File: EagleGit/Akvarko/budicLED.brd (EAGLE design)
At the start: 118.1 x 101.6 mm, 50 parts, among them IC1 7805TV, Q1 BD243C, Q2 BD243C, Q3 BD243C, Q4 BD243C, T1 2N5551, T2 2N5551, T3 2N5551, T4 2N5551, X1 SMKDSP_1,5/2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

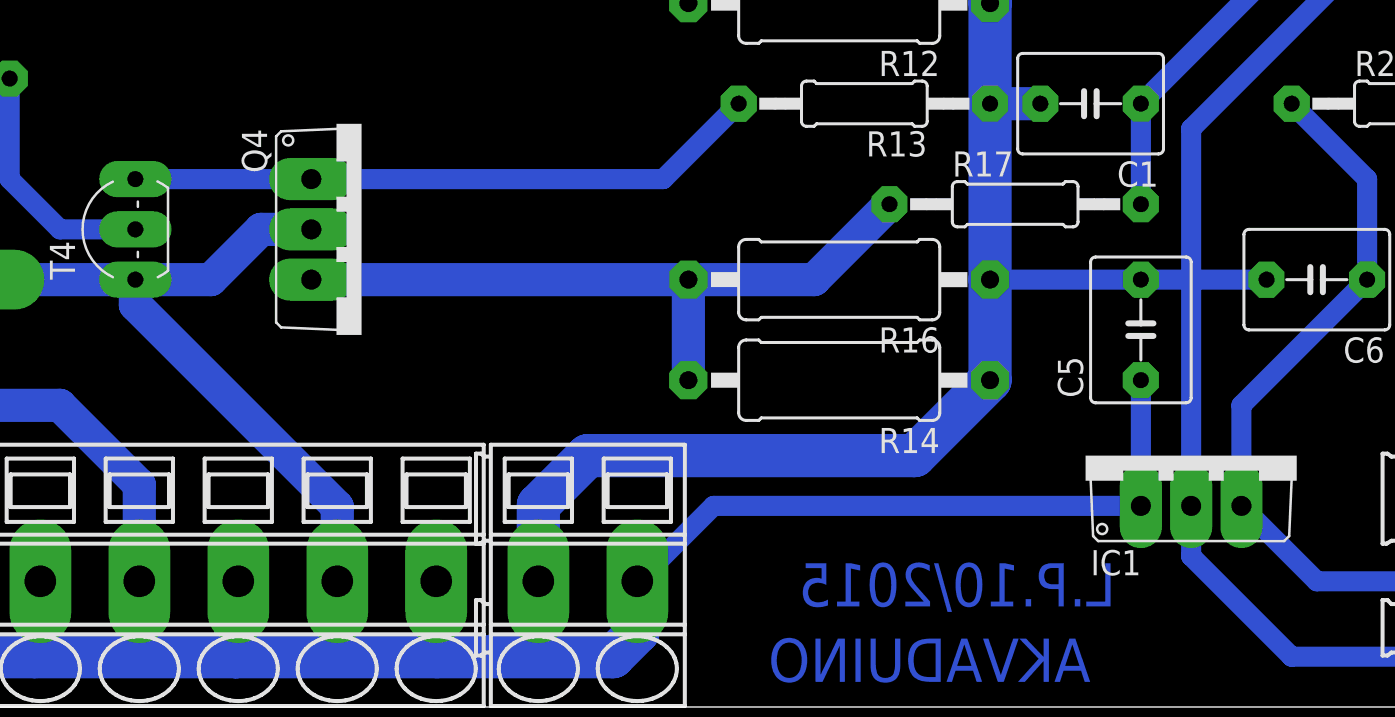
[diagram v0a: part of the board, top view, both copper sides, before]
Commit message: Vytvorena cela pro Rogowskiho civku a dodelan budic LED
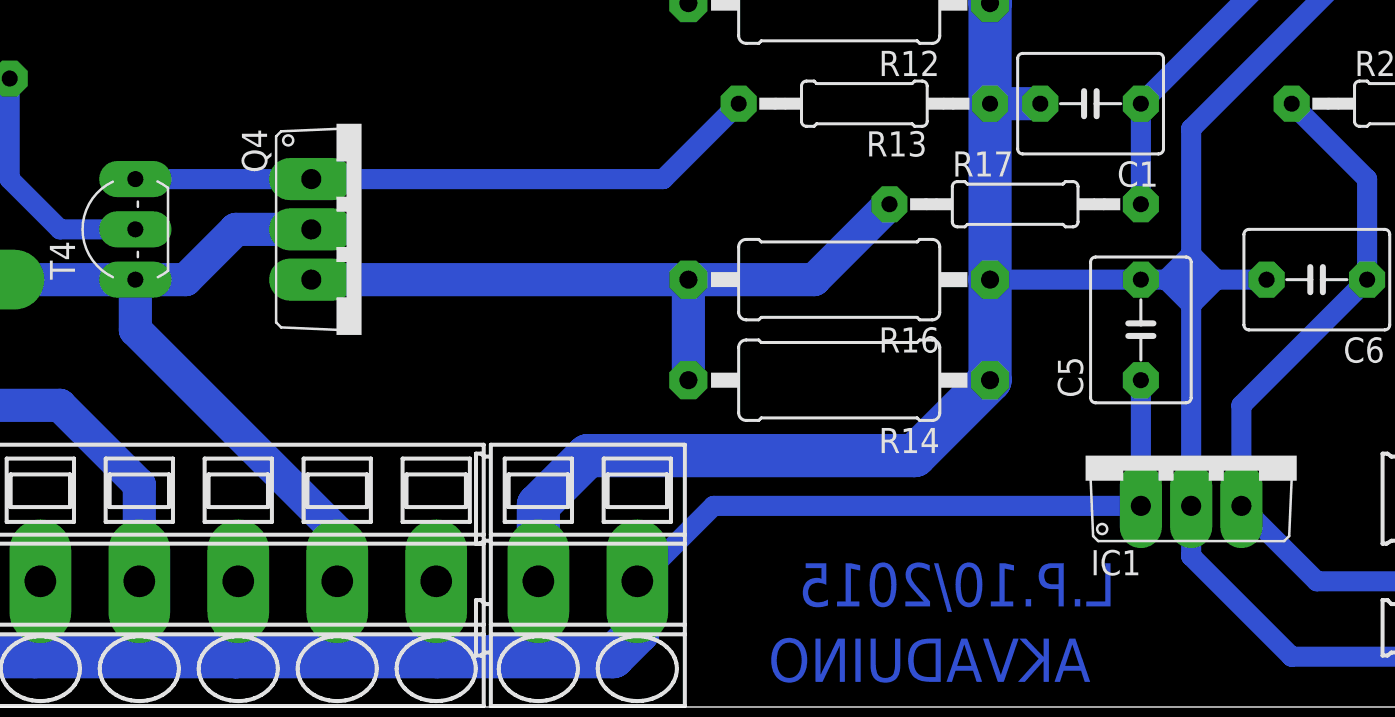
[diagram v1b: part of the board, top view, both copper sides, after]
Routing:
- net GND: track 554.0 -> 561.2 mm
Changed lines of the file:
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@@
 <contactref element="C6" pad="2"/>
 <contactref element="C7" pad="-"/>
-<wire x1="85.09" y1="21.59" x2="85.09" y2="10.16" width="1.016" layer="16"/>
+<wire x1="85.09" y1="21.59" x2="85.09" y2="20.32" width="1.016" layer="16"/>
+<wire x1="85.09" y1="20.32" x2="85.09" y2="10.16" width="1.016" layer="16"/>
 <wire x1="74.93" y1="21.59" x2="82.55" y2="21.59" width="1.016" layer="16"/>
 <wire x1="107.91" y1="6.35" x2="107.91" y2="5.04" width="1.016" layer="16"/>
@@
 <wire x1="90.17" y1="2.54" x2="85.09" y2="7.62" width="1.016" layer="16"/>
 <wire x1="85.09" y1="7.62" x2="85.09" y2="10.16" width="1.016" layer="16"/>
-<wire x1="88.9" y1="21.59" x2="85.09" y2="21.59" width="1.016" layer="16"/>
-<wire x1="85.09" y1="21.59" x2="82.55" y2="21.59" width="1.016" layer="16"/>
+<wire x1="88.9" y1="21.59" x2="86.36" y2="21.59" width="1.016" layer="16"/>
+<wire x1="86.36" y1="21.59" x2="85.09" y2="21.59" width="1.016" layer="16"/>
+<wire x1="85.09" y1="21.59" x2="83.82" y2="21.59" width="1.016" layer="16"/>
+<wire x1="83.82" y1="21.59" x2="82.55" y2="21.59" width="1.016" layer="16"/>
 <wire x1="107.91" y1="6.35" x2="107.91" y2="19.09" width="1.016" layer="16"/>
 <wire x1="107.91" y1="19.09" x2="105.41" y2="21.59" width="1.016" layer="16"/>
@@
 <wire x1="100.33" y1="95.25" x2="100.33" y2="44.45" width="1.016" layer="16"/>
 <wire x1="100.33" y1="44.45" x2="85.09" y2="29.21" width="1.016" layer="16"/>
-<wire x1="85.09" y1="29.21" x2="85.09" y2="21.59" width="1.016" layer="16"/>
+<wire x1="85.09" y1="29.21" x2="85.09" y2="22.86" width="1.016" layer="16"/>
+<wire x1="85.09" y1="22.86" x2="85.09" y2="21.59" width="1.016" layer="16"/>
 <wire x1="105.41" y1="95.25" x2="105.41" y2="21.59" width="1.016" layer="16"/>
 <contactref element="SL2" pad="1"/>
@@
 <wire x1="24.13" y1="97.79" x2="21.59" y2="97.79" width="1.016" layer="16"/>
 <wire x1="21.59" y1="97.79" x2="20.32" y2="96.52" width="1.016" layer="16"/>
+<wire x1="83.82" y1="21.59" x2="85.09" y2="22.86" width="1.016" layer="16"/>
+<wire x1="85.09" y1="22.86" x2="86.36" y2="21.59" width="1.016" layer="16"/>
+<wire x1="86.36" y1="21.59" x2="85.09" y2="20.32" width="1.016" layer="16"/>
+<wire x1="85.09" y1="20.32" x2="83.82" y2="21.59" width="1.016" layer="16"/>
 </signal>
 <signal name="N$6">
@@
 <contactref element="D4" pad="A"/>
 <wire x1="31.75" y1="21.59" x2="24.13" y2="21.59" width="1.6764" layer="16"/>
-<wire x1="40.64" y1="24.13" x2="38.1" y2="24.13" width="1.6764" layer="16"/>
-<wire x1="38.1" y1="24.13" x2="35.56" y2="21.59" width="1.6764" layer="16"/>
-<wire x1="35.56" y1="21.59" x2="31.75" y2="21.59" width="1.6764" layer="16"/>
-<wire x1="41.95" y1="6.35" x2="41.95" y2="10.12" width="1.6764" layer="16"/>
-<wire x1="41.95" y1="10.12" x2="31.75" y2="20.32" width="1.6764" layer="16"/>
-<wire x1="31.75" y1="20.32" x2="31.75" y2="21.59" width="1.6764" layer="16"/>
+<wire x1="40.64" y1="24.13" x2="36.83" y2="24.13" width="1.6764" layer="16"/>
+<wire x1="36.83" y1="24.13" x2="34.29" y2="21.59" width="1.6764" layer="16"/>
+<wire x1="34.29" y1="21.59" x2="31.75" y2="21.59" width="1.6764" layer="16"/>
+<wire x1="41.95" y1="6.35" x2="41.95" y2="8.85" width="1.6764" layer="16"/>
+<wire x1="41.95" y1="8.85" x2="31.75" y2="19.05" width="1.6764" layer="16"/>
+<wire x1="31.75" y1="19.05" x2="31.75" y2="21.59" width="1.6764" layer="16"/>
 </signal>
 <signal name="N$13">
